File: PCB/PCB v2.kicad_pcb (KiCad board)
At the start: 4 copper layers, 56 x 45 mm, 132 parts, among them J2 USB_C_Receptacle_PowerOnly_6P, J3 6871XX182122_687110182122, J5 Conn_01x03_Pin, J7 Conn_02x06_Odd_Even, U1 TPD2E2U06DCK, U11 OPA4350EA_250, U12 OPA4350EA_250, U13 OPA4350EA_250, U2 ADS131M08xPBS, U3 74LVC1G17, U4 LM27762, U6 OPA4350EA_250, U7 LP5907MFX-3.3

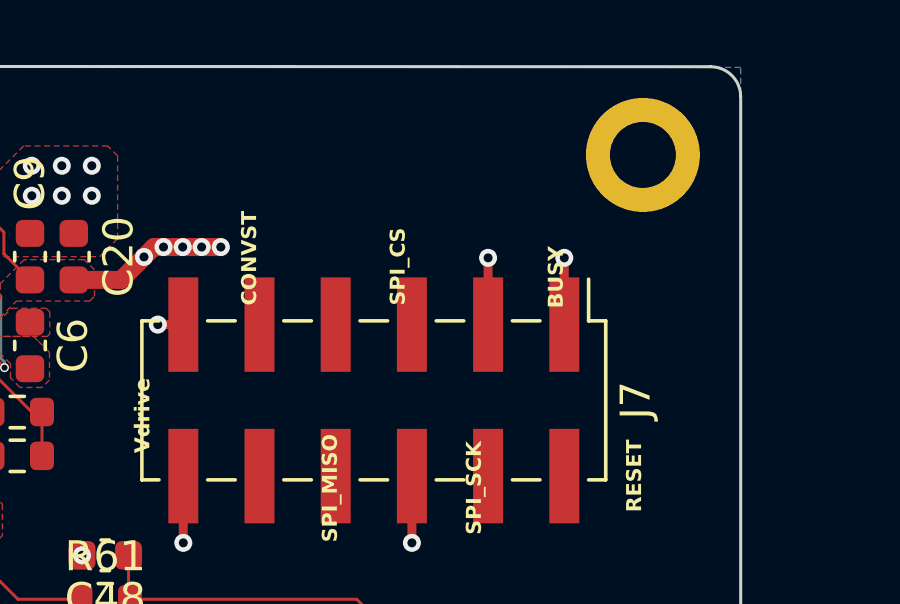
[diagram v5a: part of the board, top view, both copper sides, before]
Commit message: Re-pin J7 (MCU header) to match U2's digital pin order
The clock and the six ADC digital lines enter U2 (ADS131M08) from its
right side. From top to bottom they arrive as CLKIN (via U3/R80), DIN,
DOUT (via R81), SCLK, DRDY (via R82) and CS, with SYNC at the bottom
corner. With the old J7 order the F.Cu fan-out to the header crossed
itself. Moving digital lines to B.Cu is not an option, because B.Cu
sits over the +2V5 analog plane.

The new order lets the lines run up the right board edge and enter J7
from the side:
- DIN, MISO, SCLK, DRDY and CS go through the 1.9 mm gap between the
  two pad rows. They peel off down into the bottom row or up into the
  top row in the order they arrive.
- SYNC reaches pad 1 from the side.
- MCU_CLK stays on pin 2, directly above U3.

  pin  before           after
   1   GND              ADC_SYNC_RESET
   4   ADC_SCLK         ADC_MOSI
   5   ADC_MOSI         ADC_CS
   7   ADC_MISO         GND
   8   ADC_CS           ADC_MISO
  10   ADC_SYNC_RESET   ADC_SCLK
  (2 MCU_CLK, 3/6/11/12 GND and 9 ADC_DRDY unchanged)

- There are still 5 GND pins. MCU_CLK keeps GND on pin 3 as its
  ribbon-cable neighbour; its other neighbour, pin 1, is SYNC_RESET,
  which rarely switches.
- The MCU-side wiring must follow this table (CHANGELOG Part 8).

Schematic (FOGLIO1):
- Pin 1's tie to pin 3's GND is removed (wire and junction). Pin 3
  keeps its own GND symbol (#PWR0160 moved), and pin 1 gets an
  ADC_SYNC_RESET label.
- Pin 7's ADC_MISO label is replaced by a GND symbol (#PWR0243, new).
- The other labels are renamed in place.
- Netlist: only J7's pin memberships change. ERC: 0 errors, with the
  same 31 warnings as before.

PCB:
- The J7 pad nets are updated to match, so Update PCB from Schematic
  has nothing to change.
- Pin 1's GND stub and via are removed. Pin 7 gets a GND stub and a via
  past its outer end at (163.76, 82.43).
- DRC: identical to the previous commit.

Co-Authored-By: Claude Opus 5.5 <noreply@anthropic.com>
Claude-Session: http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
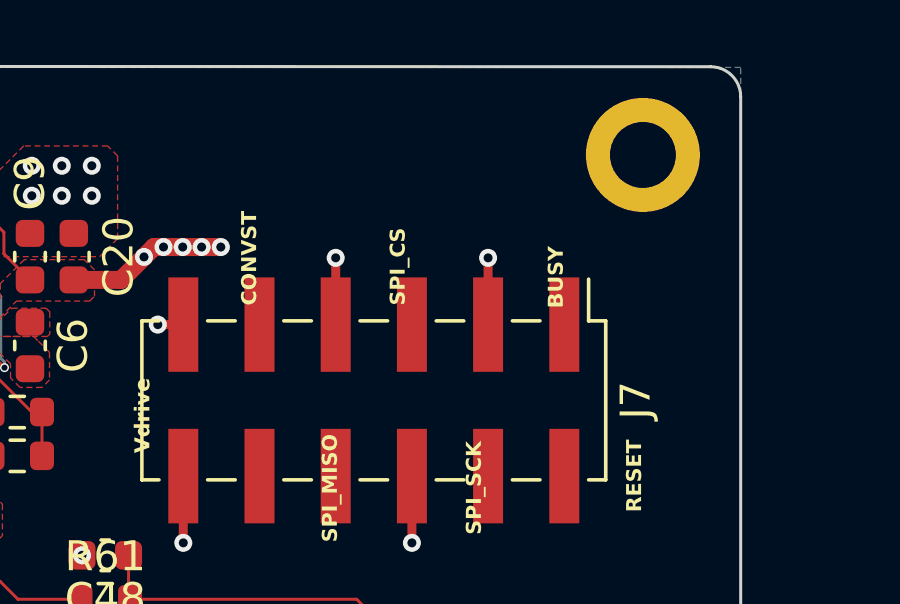
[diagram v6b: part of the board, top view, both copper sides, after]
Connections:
- J7 pad 1: GND -> /POWER SUPPLY - ADC - SACRIFIED SENSOR/ADC_SYNC_RESET
- J7 pad 10: /POWER SUPPLY - ADC - SACRIFIED SENSOR/ADC_SYNC_RESET -> /POWER SUPPLY - ADC - SACRIFIED SENSOR/ADC_SCLK
- J7 pad 4: /POWER SUPPLY - ADC - SACRIFIED SENSOR/ADC_SCLK -> /POWER SUPPLY - ADC - SACRIFIED SENSOR/ADC_MOSI
- J7 pad 5: /POWER SUPPLY - ADC - SACRIFIED SENSOR/ADC_MOSI -> /POWER SUPPLY - ADC - SACRIFIED SENSOR/ADC_CS
- J7 pad 7: /POWER SUPPLY - ADC - SACRIFIED SENSOR/ADC_MISO -> GND
- J7 pad 8: /POWER SUPPLY - ADC - SACRIFIED SENSOR/ADC_CS -> /POWER SUPPLY - ADC - SACRIFIED SENSOR/ADC_MISO
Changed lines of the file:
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@@
 			(size 3.15 1)
 			(layers "F.Cu" "F.Mask" "F.Paste")
-			(net "GND")
+			(net "/POWER SUPPLY - ADC - SACRIFIED SENSOR/ADC_SYNC_RESET")
 			(pinfunction "Pin_1_1")
 			(pintype "passive")
@@
 			(size 3.15 1)
 			(layers "F.Cu" "F.Mask" "F.Paste")
-			(net "/POWER SUPPLY - ADC - SACRIFIED SENSOR/ADC_SCLK")
+			(net "/POWER SUPPLY - ADC - SACRIFIED SENSOR/ADC_MOSI")
 			(pinfunction "Pin_4_4")
 			(pintype "passive")
@@
 			(size 3.15 1)
 			(layers "F.Cu" "F.Mask" "F.Paste")
-			(net "/POWER SUPPLY - ADC - SACRIFIED SENSOR/ADC_MOSI")
+			(net "/POWER SUPPLY - ADC - SACRIFIED SENSOR/ADC_CS")
 			(pinfunction "Pin_5_5")
 			(pintype "passive")
@@
 			(size 3.15 1)
 			(layers "F.Cu" "F.Mask" "F.Paste")
-			(net "/POWER SUPPLY - ADC - SACRIFIED SENSOR/ADC_MISO")
+			(net "GND")
 			(pinfunction "Pin_7_7")
 			(pintype "passive")
@@
 			(size 3.15 1)
 			(layers "F.Cu" "F.Mask" "F.Paste")
-			(net "/POWER SUPPLY - ADC - SACRIFIED SENSOR/ADC_CS")
+			(net "/POWER SUPPLY - ADC - SACRIFIED SENSOR/ADC_MISO")
 			(pinfunction "Pin_8_8")
 			(pintype "passive")
@@
 			(size 3.15 1)
 			(layers "F.Cu" "F.Mask" "F.Paste")
-			(net "/POWER SUPPLY - ADC - SACRIFIED SENSOR/ADC_SYNC_RESET")
+			(net "/POWER SUPPLY - ADC - SACRIFIED SENSOR/ADC_SCLK")
 			(pinfunction "Pin_10_10")
 			(pintype "passive")
@@
 	)
 	(segment
-		(start 171.38 84.655)
-		(end 171.38 82.43)
-		(width 0.3)
-		(layer "F.Cu")
-		(net "GND")
-	)
-	(segment
 		(start 122.89 99.5)
 		(end 122.89 100.050903)
@@
 	)
 	(via
-		(at 171.38 82.43)
-		(size 0.6)
-		(drill 0.3)
-		(layers "F.Cu" "B.Cu")
-		(net "GND")
-	)
-	(via
 		(at 130.2 119.6)
 		(size 0.6)
@@
 	)
 	(embedded_fonts no)
+	(segment
+		(start 163.76 84.655)
+		(end 163.76 82.43)
+		(width 0.3)
+		(layer "F.Cu")
+		(net "GND")
+	)
+	(via
+		(at 163.76 82.43)
+		(size 0.6)
+		(drill 0.3)
+		(layers "F.Cu" "B.Cu")
+		(net "GND")
+	)
 )

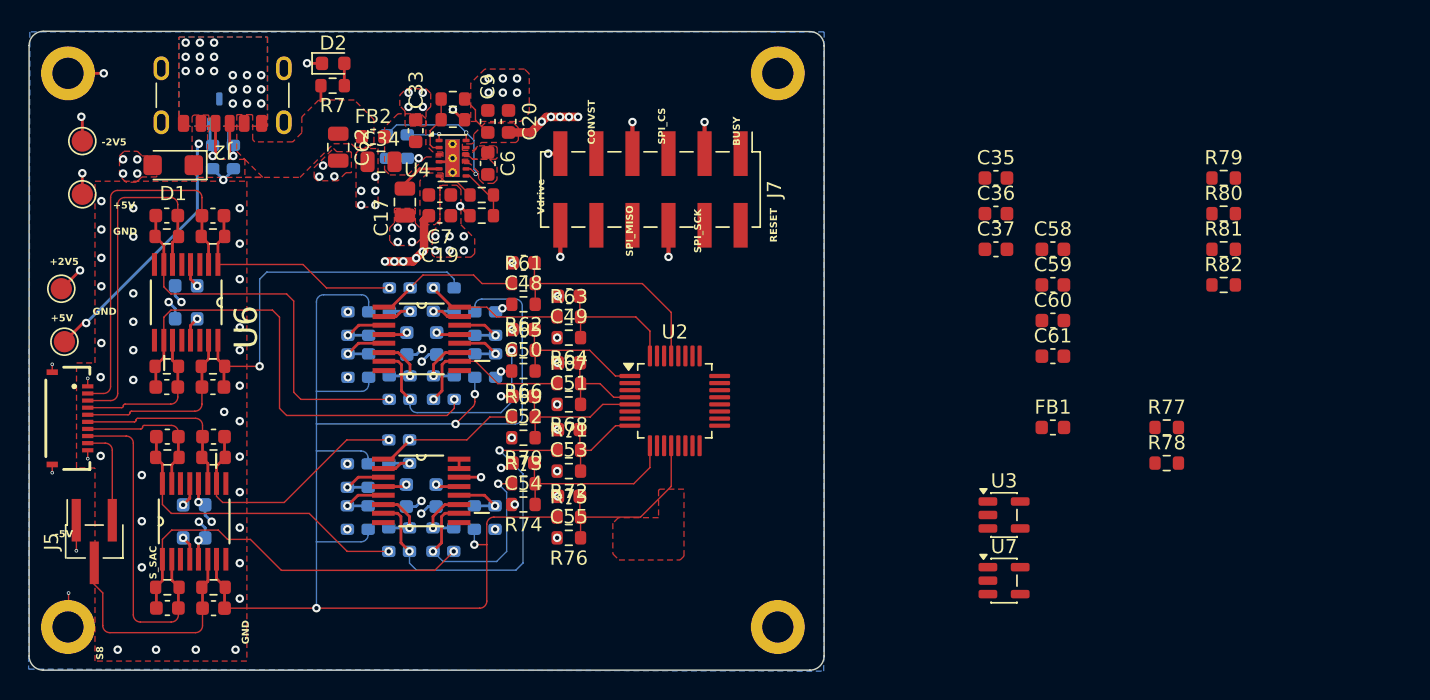
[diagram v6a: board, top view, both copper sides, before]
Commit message: Place and route the ADC area: clock buffer, decoupling, SPI to J7
Board is now fully connected (DRC: 0 unconnected items).

ADC position (moved in pcbnew): U2 at (166.13, 102.10), 0.6 mm left of
the earlier spot, with the AIN fan-in adjusted. This widens the strip
right of U2 to 7.0 mm.

Placement:
- Clock buffer group, all within x <= 174.55, leaving the strip on the
  right edge free for the digital lines:
  - U3 74LVC1G17 at (172.75, 97.9), rotated 0.
  - R79 100k clock pull-down at (171.5, 94.0).
  - C58 at (173.9, 94.55), vertical, above U3's VCC pin.
  - R80 33R at (173.05, 100.85), source termination at U3's output,
    with its CLKIN pad level with U2 pin 23.
- U2 decoupling: C35 (CAP, pin 24) and C36 (DVDD, pin 26) above U2's
  top-right corner, placed and rotated in pcbnew. C37 (AVDD, pin 15) and
  C59 (REFIN, pin 14) below the bottom-right corner.
- R81/R82 (33R on DOUT/DRDY) are staggered at (172.3, 102.65) and
  (173.3, 104.2), which opens a lane for SCLK between them.
- FB1 (+3.3VA to +3V3), R78 (SYNC pull-up) and R77 (CS pull-up) sit at
  the bottom-right.
- Courtyards are kept clear of U2 and of J7, whose courtyard reaches
  down to y 93.05.

Supplies:
- +3.3VA from the U7 LDO: the F.Cu run through J7's row gap and down the
  right edge is removed. It now drops to B.Cu at x 152.5 (0.4 mm), runs
  along y 91, down under U2 at x 164.8, and up beside C37. Short F.Cu
  runs feed C37 and FB1.
- +3V3 (FB1 out): F.Cu to R78 and R77, then B.Cu up x 174.5 to a via
  at U3/C58, and along y 96.1 to a via beside C36 for DVDD.

Digital (0.1 mm, F.Cu, over the In1 GND plane 0.1 mm below):
- DIN, MISO (through R81), SCLK, DRDY (through R82) and CS fan out from
  U2's right pins, go up the right edge at x 174.9-176.5 (0.4 mm
  pitch), and run through J7's row gap into pads 4, 8, 10, 5 and 9,
  with no crossings.
- SYNC: F.Cu from pin 16 to R78, then B.Cu around the bottom and up
  the right edge (it barely switches), back up to F.Cu to enter J7 pad 1
  from the side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
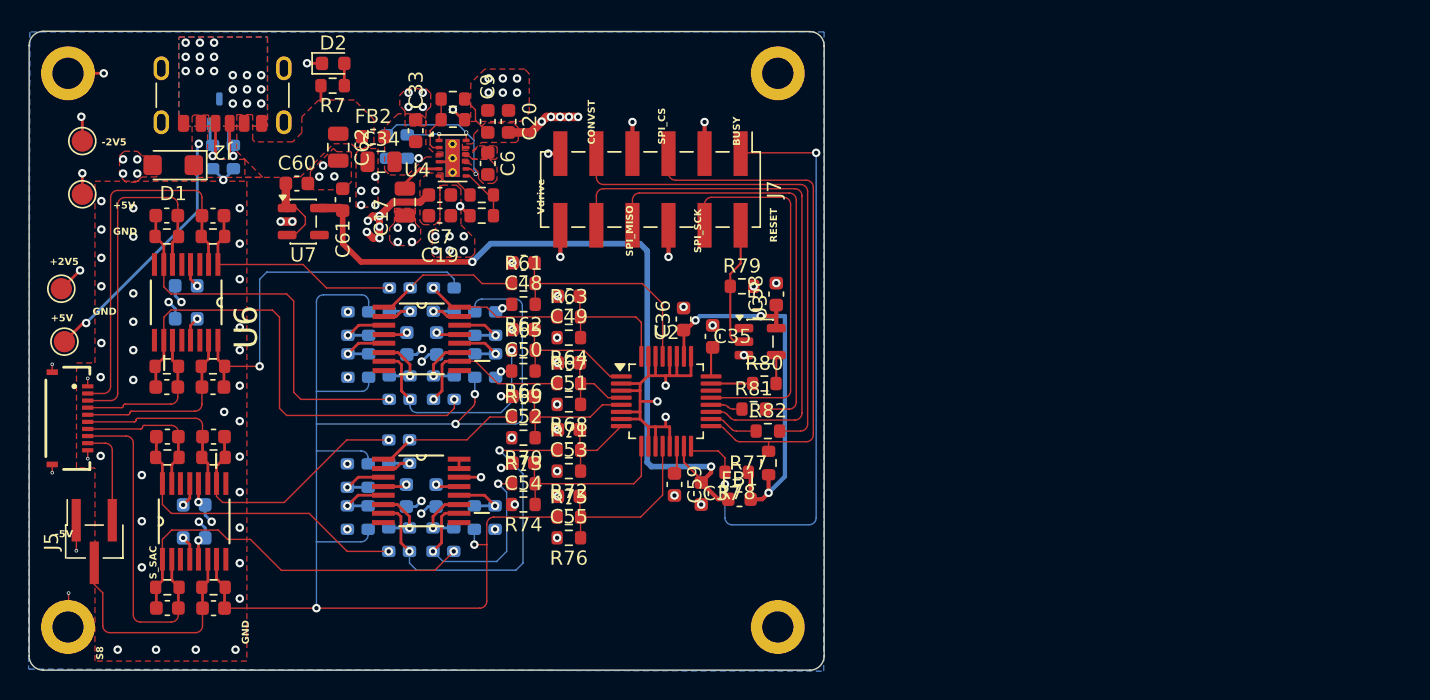
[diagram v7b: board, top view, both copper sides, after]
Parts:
- moved U7 55.5 mm to (140.6, 89.4)
- moved C60 54.1 mm to (140.1, 86.8)
- moved C61 51.2 mm to (143.3, 87.9), turned to 90 degrees
- moved R81 35.0 mm to (172.3, 102.7)
- moved R79 34.8 mm to (171.5, 94.0)
- moved R80 34.5 mm to (173.1, 100.9)
- moved R82 33.7 mm to (173.3, 104.2)
- moved R78 30.3 mm to (171.1, 107.1), turned to 180 degrees
- moved C59 30.1 mm to (166.7, 108.0), turned to -90 degrees
- moved R77 28.2 mm to (173.3, 106.5), turned to 90 degrees
- moved C37 27.0 mm to (168.6, 108.6), turned to -90 degrees
- moved C36 23.2 mm to (167.4, 96.3), turned to 90 degrees
- moved C35 22.9 mm to (169.4, 97.5), turned to 90 degrees
- moved FB1 22.6 mm to (171.3, 109.0)
- moved U3 21.1 mm to (172.8, 97.9)
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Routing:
- net +3.3VA: track 0.00 -> 53.1 mm, vias 0 -> 2
- net /POWER SUPPLY - ADC - SACRIFIED SENSOR/ADC_SYNC_RESET: track 0.00 -> 45.1 mm, vias 0 -> 2
- net /POWER SUPPLY - ADC - SACRIFIED SENSOR/ADC_SCLK: track 0.00 -> 39.2 mm
- net /POWER SUPPLY - ADC - SACRIFIED SENSOR/ADC_CS: track 0.00 -> 38.1 mm
- net /POWER SUPPLY - ADC - SACRIFIED SENSOR/ADC_DRDY: track 0.00 -> 35.7 mm
- net /POWER SUPPLY - ADC - SACRIFIED SENSOR/ADC_MISO: track 0.00 -> 30.5 mm
- net +3V3: track 0.00 -> 29.7 mm, vias 0 -> 3
- net GND: track 42.1 -> 69.6 mm, vias 132 -> 144
- net /POWER SUPPLY - ADC - SACRIFIED SENSOR/ADC_MOSI: track 0.00 -> 27.1 mm
- net /POWER SUPPLY - ADC - SACRIFIED SENSOR/MCU_CLK: track 0.00 -> 9.23 mm
- net +5V: track 19.1 -> 24.5 mm
- net /POWER SUPPLY - ADC - SACRIFIED SENSOR/U2_DRDY: track 0.00 -> 3.48 mm
- net Net-(U2-XTAL1/CLKIN): track 0.00 -> 2.93 mm
- net /POWER SUPPLY - ADC - SACRIFIED SENSOR/U2_DOUT: track 0.00 -> 2.25 mm
- net Net-(U2-CAP): track 0.00 -> 2.09 mm
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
